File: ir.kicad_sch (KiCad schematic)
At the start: 38 parts

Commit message: placement done
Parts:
- D?: footprint LED_SMD:LED_0603_1608Metric_Pad1.05x0.95mm_HandSolder -> footprints:led0603
- SW?: footprint Button_Switch_SMD:SW_Push_SPST_NO_Alps_SKRK -> footprints:SW_PUSH_SPST
- U? (x24): footprint OptoDevice:Vishay_MINICAST-3Pin -> footprints:Vishay_MINICAST-3P
- Y?: footprint Crystal:Crystal_SMD_5032-2Pin_5.0x3.2mm -> footprints:Crystal
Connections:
- net IR1: now also U?.15 (PA5); no longer U?.29 (PA8)
- net IR10: now also U?.32 (PA11); no longer U?.10 (PA0)
- net IR11: now also U?.33 (PA12); no longer U?.11 (PA1)
- net IR12: now also U?.38 (PA15); no longer U?.12 (PA2)
- net IR13: now also U?.39 (PB3); no longer U?.13 (PA3)
- net IR14: now also U?.40 (PB4); no longer U?.14 (PA4)
- net IR15: now also U?.41 (PB5); no longer U?.15 (PA5)
- net IR16: now also U?.42 (PB6); no longer U?.16 (PA6)
- net IR17: now also U?.43 (PB7); no longer U?.17 (PA7)
- net IR18: now also U?.45 (PB8); no longer U?.18 (PB0)
- net IR19: now also U?.46 (PB9); no longer U?.19 (PB1)
- net IR2: now also U?.16 (PA6); no longer U?.38 (PA15)
- net IR20: now also U?.10 (PA0); no longer U?.20 (PB2)
- net IR21: now also U?.11 (PA1); no longer U?.25 (PB12)
- net IR22: now also U?.12 (PA2); no longer U?.26 (PB13)
- net IR23: now also U?.13 (PA3); no longer U?.27 (PB14)
- net IR24: now also U?.14 (PA4); no longer U?.28 (PB15)
- net IR3: now also U?.17 (PA7); no longer U?.39 (PB3)
- net IR4: now also U?.18 (PB0); no longer U?.40 (PB4)
- net IR5: now also U?.19 (PB1); no longer U?.41 (PB5)
- net IR6: now also U?.21 (PB10); no longer U?.42 (PB6)
- net IR7: now also U?.27 (PB14); no longer U?.43 (PB7)
- net IR8: now also U?.28 (PB15); no longer U?.45 (PB8)
- net IR9: now also U?.29 (PA8); no longer U?.46 (PB9)
- no-connect marks 5 -> 6

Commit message: e
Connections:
- net IR6: now also U?.20 (PB2); no longer U?.21 (PB10)
- no-connect marks 6 -> 7
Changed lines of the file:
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@@
   (no_connect (at 232.41 123.19))
   (no_connect (at 245.11 57.15))
+  (no_connect (at 232.41 115.57))
   (no_connect (at 232.41 82.55))
   (wire (pts (xy 58.42 57.15) (xy 66.04 57.15))
@@
     (stroke (width 0) (type default))
   )
-  (wire (pts (xy 226.06 115.57) (xy 232.41 115.57))
-    (stroke (width 0) (type default))
-  )
   (wire (pts (xy 96.52 41.91) (xy 104.14 41.91))
     (stroke (width 0) (type default))
@@
     (stroke (width 0) (type default))
   )
+  (wire (pts (xy 226.06 95.25) (xy 232.41 95.25))
+    (stroke (width 0) (type default))
+  )
   (wire (pts (xy 247.65 55.88) (xy 252.73 55.88))
     (stroke (width 0) (type default))
@@
     (effects (font (size 1.27 1.27)) (justify left bottom))
   )
+  (label "IR6" (at 227.33 95.25 0) (fields_autoplaced)
+    (effects (font (size 1.27 1.27)) (justify left bottom))
+  )
   (label "IR15" (at 137.16 119.38 0) (fields_autoplaced)
     (effects (font (size 1.27 1.27)) (justify left bottom))
@@
     (effects (font (size 1.27 1.27)) (justify left bottom))
   )
-  (label "IR6" (at 227.33 115.57 0) (fields_autoplaced)
-    (effects (font (size 1.27 1.27)) (justify left bottom))
-  )

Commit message: e
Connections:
- net SWCLK: now also J?.2 (Pin_2); no longer J?.3 (Pin_3)
- net SWDIO: now also J?.3 (Pin_3); no longer J?.2 (Pin_2)
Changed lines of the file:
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@@
+    (effects (font (size 1.27 1.27)) (justify left bottom))
+  )
+  (label "SWDIO" (at 233.68 153.67 0) (fields_autoplaced)
     (effects (font (size 1.27 1.27)) (justify left bottom))
   )
   (label "IR5" (at 227.33 92.71 0) (fields_autoplaced)
+    (effects (font (size 1.27 1.27)) (justify left bottom))
+  )
+  (label "SWCLK" (at 233.68 151.13 0) (fields_autoplaced)
     (effects (font (size 1.27 1.27)) (justify left bottom))
   )
@@
   (label "IR24" (at 270.51 72.39 180) (fields_autoplaced)
     (effects (font (size 1.27 1.27)) (justify right bottom))
-  )
-  (label "SWDIO" (at 233.68 151.13 0) (fields_autoplaced)
-    (effects (font (size 1.27 1.27)) (justify left bottom))
   )
   (label "IR8" (at 97.79 77.47 0) (fields_autoplaced)
@@
     (effects (font (size 1.27 1.27)) (justify left bottom))
   )
-  (label "SWCLK" (at 233.68 153.67 0) (fields_autoplaced)
-    (effects (font (size 1.27 1.27)) (justify left bottom))
-  )

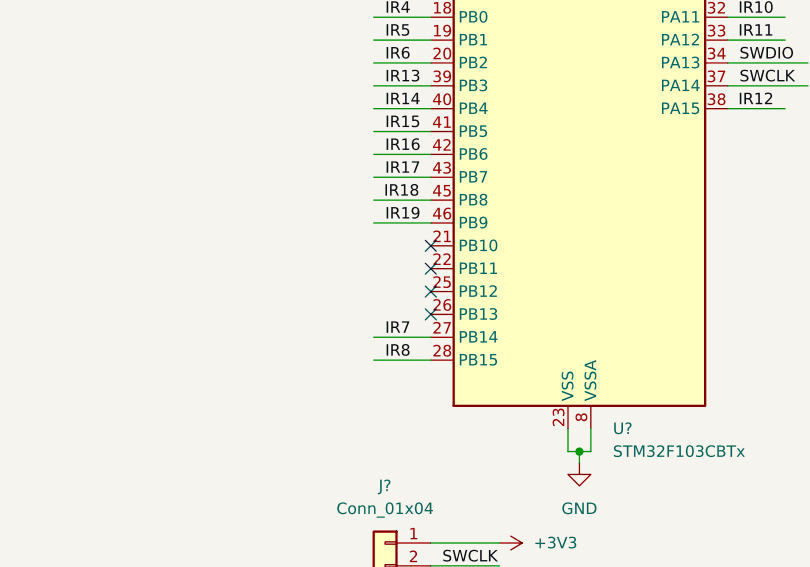
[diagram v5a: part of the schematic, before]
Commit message: left with power and sw
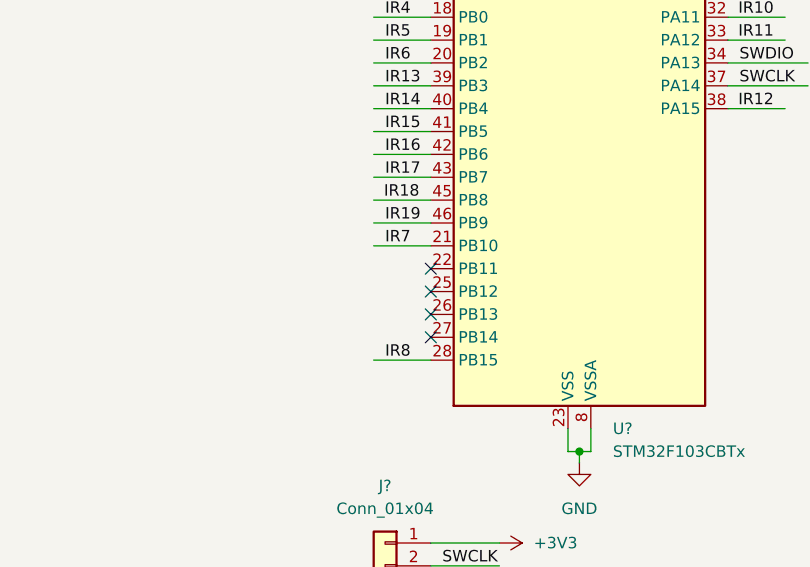
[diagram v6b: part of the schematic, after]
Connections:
- net IR7: now also U?.21 (PB10); no longer U?.27 (PB14)
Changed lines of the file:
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@@
   (no_connect (at 232.41 118.11))
   (no_connect (at 232.41 85.09))
+  (no_connect (at 232.41 125.73))
   (no_connect (at 232.41 123.19))
   (no_connect (at 245.11 57.15))
-  (no_connect (at 232.41 115.57))
   (no_connect (at 232.41 82.55))
   (wire (pts (xy 58.42 57.15) (xy 66.04 57.15))
@@
     (stroke (width 0) (type default))
   )
-  (wire (pts (xy 226.06 125.73) (xy 232.41 125.73))
-    (stroke (width 0) (type default))
-  )
   (wire (pts (xy 224.79 62.23) (xy 232.41 62.23))
     (stroke (width 0) (type default))
@@
     (stroke (width 0) (type default))
   )
+  (wire (pts (xy 226.06 115.57) (xy 232.41 115.57))
+    (stroke (width 0) (type default))
+  )
   (wire (pts (xy 135.89 62.23) (xy 143.51 62.23))
     (stroke (width 0) (type default))
@@
     (effects (font (size 1.27 1.27)) (justify right bottom))
   )
-  (label "IR7" (at 227.33 125.73 0) (fields_autoplaced)
-    (effects (font (size 1.27 1.27)) (justify left bottom))
-  )
+  (label "IR7" (at 227.33 115.57 0) (fields_autoplaced)
+    (effects (font (size 1.27 1.27)) (justify left bottom))
+  )

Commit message: i wanna kill myself
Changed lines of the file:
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@@
     (effects (font (size 1.27 1.27)) (justify right bottom))
-  )
-  (global_label "IR RX" (shape bidirectional) (at 274.32 85.09 0)
-    (effects (font (size 1.27 1.27)) (justify left))
-    (property "Intersheetrefs" "${INTERSHEET_REFS}" (at 282.2141 85.09 0)
-      (effects (font (size 1.27 1.27)) hide)
-    )
-  )
-  (global_label "IR TX" (shape bidirectional) (at 274.32 87.63 0)
-    (effects (font (size 1.27 1.27)) (justify left))
-    (property "Intersheetrefs" "${INTERSHEET_REFS}" (at 282.2141 87.63 0)
-      (effects (font (size 1.27 1.27)) hide)
-    )
   )
   (symbol (lib_id "Device:C") (at 204.47 69.85 270) (unit 1)
